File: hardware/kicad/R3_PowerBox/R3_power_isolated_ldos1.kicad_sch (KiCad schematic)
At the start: 12 parts, among them U4 ADM7150ACPZ-3.3-R7, U5 TPS7A2033PDBVR

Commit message: Finalize R3 PowerBox pre-placement corrections
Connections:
- net N$15 is gone; now on net N$14: C44.1, U4.3 (BYP)
- net N$14: no longer C41.1, U4.1 (VREG)
- new net N$13: C41.1, U4.1 (VREG)

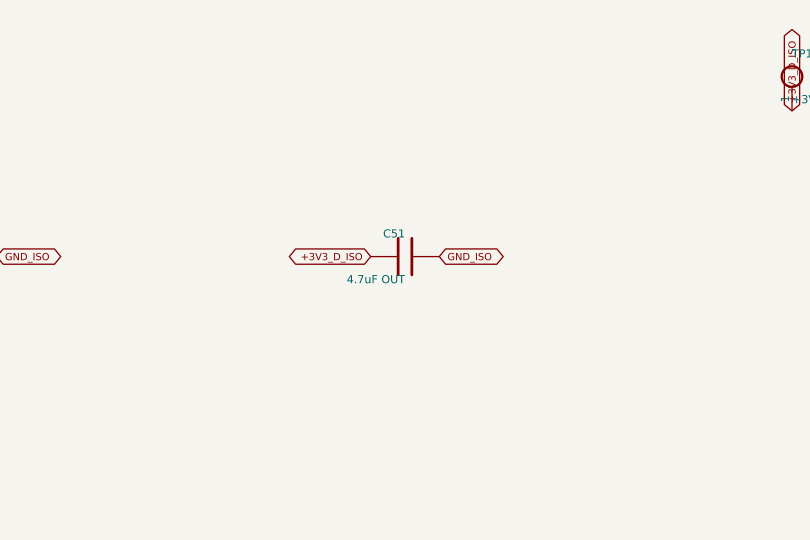
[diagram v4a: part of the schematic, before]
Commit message: Finish R3 PowerBox routing checkpoint F and verification
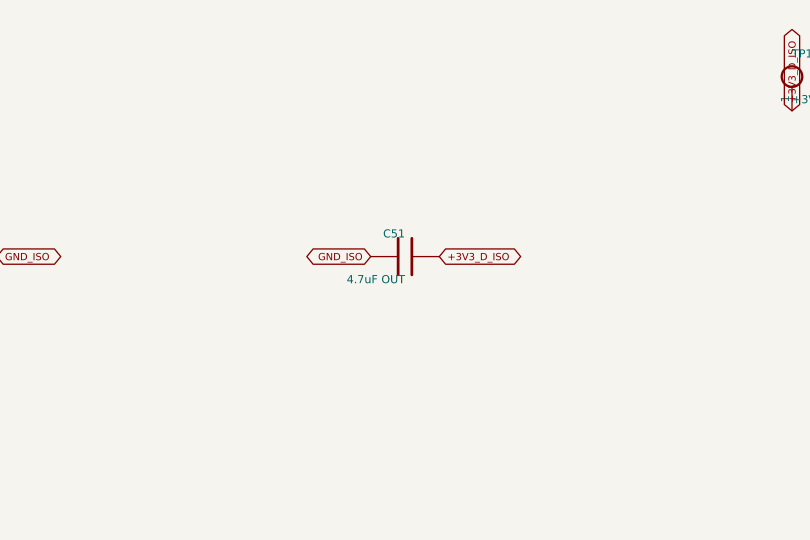
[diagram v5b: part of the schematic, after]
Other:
- moved on the sheet: C51
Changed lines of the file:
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@@
 	(global_label "+3V3_D_ISO"
+		(shape bidirectional)
+		(at 198.81 68 0)
+		(effects
+			(font
+				(size 0.8 0.8)
+			)
+			(justify left)
+		)
+	)
+	(global_label "GND_ISO"
 		(shape bidirectional)
 		(at 191.19 68 180)
@@
 			)
 			(justify right)
-		)
-	)
-	(global_label "GND_ISO"
-		(shape bidirectional)
-		(at 198.81 68 0)
-		(effects
-			(font
-				(size 0.8 0.8)
-			)
-			(justify left)
 		)
 	)
@@
     (instances
       (project "SKiDL-Generated"
-        (path "/9be6bff1-dc85-4a48-94a9-d7223c5e518f/851a1ce1-50e3-53b2-8137-9c4e81a721ef"
+        (path "/c950aac3-a7f8-40a1-8854-63ca2e6194cc/851a1ce1-50e3-53b2-8137-9c4e81a721ef"
           (reference "#FLG0301")
           (unit 1)))))
@@
     (instances
       (project "SKiDL-Generated"
-        (path "/9be6bff1-dc85-4a48-94a9-d7223c5e518f/851a1ce1-50e3-53b2-8137-9c4e81a721ef"
+        (path "/c950aac3-a7f8-40a1-8854-63ca2e6194cc/851a1ce1-50e3-53b2-8137-9c4e81a721ef"
           (reference "#FLG0302")
           (unit 1)))))
@@
     (instances
       (project "SKiDL-Generated"
-        (path "/9be6bff1-dc85-4a48-94a9-d7223c5e518f/851a1ce1-50e3-53b2-8137-9c4e81a721ef"
+        (path "/c950aac3-a7f8-40a1-8854-63ca2e6194cc/851a1ce1-50e3-53b2-8137-9c4e81a721ef"
           (reference "U4")
           (unit 1)))))
@@
     (instances
       (project "SKiDL-Generated"
-        (path "/9be6bff1-dc85-4a48-94a9-d7223c5e518f/851a1ce1-50e3-53b2-8137-9c4e81a721ef"
+        (path "/c950aac3-a7f8-40a1-8854-63ca2e6194cc/851a1ce1-50e3-53b2-8137-9c4e81a721ef"
           (reference "R40")
           (unit 1)))))
@@
     (instances
       (project "SKiDL-Generated"
-        (path "/9be6bff1-dc85-4a48-94a9-d7223c5e518f/851a1ce1-50e3-53b2-8137-9c4e81a721ef"
+        (path "/c950aac3-a7f8-40a1-8854-63ca2e6194cc/851a1ce1-50e3-53b2-8137-9c4e81a721ef"
           (reference "C40")
           (unit 1)))))
@@
     (instances
       (project "SKiDL-Generated"
-        (path "/9be6bff1-dc85-4a48-94a9-d7223c5e518f/851a1ce1-50e3-53b2-8137-9c4e81a721ef"
+        (path "/c950aac3-a7f8-40a1-8854-63ca2e6194cc/851a1ce1-50e3-53b2-8137-9c4e81a721ef"
           (reference "C41")
           (unit 1)))))
@@
     (instances
       (project "SKiDL-Generated"
-        (path "/9be6bff1-dc85-4a48-94a9-d7223c5e518f/851a1ce1-50e3-53b2-8137-9c4e81a721ef"
+        (path "/c950aac3-a7f8-40a1-8854-63ca2e6194cc/851a1ce1-50e3-53b2-8137-9c4e81a721ef"
           (reference "C42")
           (unit 1)))))
@@
     (instances
       (project "SKiDL-Generated"
-        (path "/9be6bff1-dc85-4a48-94a9-d7223c5e518f/851a1ce1-50e3-53b2-8137-9c4e81a721ef"
+        (path "/c950aac3-a7f8-40a1-8854-63ca2e6194cc/851a1ce1-50e3-53b2-8137-9c4e81a721ef"
           (reference "C43")
           (unit 1)))))
@@
     (instances
       (project "SKiDL-Generated"
-        (path "/9be6bff1-dc85-4a48-94a9-d7223c5e518f/851a1ce1-50e3-53b2-8137-9c4e81a721ef"
+        (path "/c950aac3-a7f8-40a1-8854-63ca2e6194cc/851a1ce1-50e3-53b2-8137-9c4e81a721ef"
           (reference "C44")
           (unit 1)))))
@@
     (instances
       (project "SKiDL-Generated"
-        (path "/9be6bff1-dc85-4a48-94a9-d7223c5e518f/851a1ce1-50e3-53b2-8137-9c4e81a721ef"
+        (path "/c950aac3-a7f8-40a1-8854-63ca2e6194cc/851a1ce1-50e3-53b2-8137-9c4e81a721ef"
           (reference "U5")
           (unit 1)))))
@@
     (instances
       (project "SKiDL-Generated"
-        (path "/9be6bff1-dc85-4a48-94a9-d7223c5e518f/851a1ce1-50e3-53b2-8137-9c4e81a721ef"
+        (path "/c950aac3-a7f8-40a1-8854-63ca2e6194cc/851a1ce1-50e3-53b2-8137-9c4e81a721ef"
           (reference "C50")
           (unit 1)))))
   (symbol
     (lib_id "R3_POWER_GEN:C")
-    (at 195 68 90)
+    (at 195 68 270)
     (unit 1)
     (exclude_from_sim no)
@@
     (fields_autoplaced yes)
     (property "Reference" "C51"
-      (at 195 65.46 90)
+      (at 195 65.46 270)
       (effects
         (font
@@
         (justify left)))
     (property "Value" "4.7uF OUT"
-      (at 195 70.54 90)
+      (at 195 70.54 270)
       (effects
         (font
@@
         (justify left)))
     (property "Footprint" "Capacitor_SMD:C_0603_1608Metric"
-      (at 195 68 90)
-      (effects
-        (font
-          (size 0.9 0.9))
-        (hide yes)))
-    (property "Datasheet" "~"
-      (at 195 68 90)
-      (effects
-        (font
-          (size 0.9 0.9))
-        (hide yes)))
-    (property "Description" ""
-      (at 195 68 90)
-      (effects
-        (font
-          (size 0.9 0.9))
-        (hide yes)))
-    (pin "1"
-)
-    (pin "2"
-)
-    (instances
-      (project "SKiDL-Generated"
-        (path "/9be6bff1-dc85-4a48-94a9-d7223c5e518f/851a1ce1-50e3-53b2-8137-9c4e81a721ef"
+      (at 195 68 270)
+      (effects
+        (font
+          (size 0.9 0.9))
+        (hide yes)))
+    (property "Datasheet" "~"
+      (at 195 68 270)
+      (effects
+        (font
+          (size 0.9 0.9))
+        (hide yes)))
+    (property "Description" ""
+      (at 195 68 270)
+      (effects
+        (font
+          (size 0.9 0.9))
+        (hide yes)))
+    (pin "1"
+)
+    (pin "2"
+)
+    (instances
+      (project "SKiDL-Generated"
+        (path "/c950aac3-a7f8-40a1-8854-63ca2e6194cc/851a1ce1-50e3-53b2-8137-9c4e81a721ef"
           (reference "C51")
           (unit 1)))))
@@
     (instances
       (project "SKiDL-Generated"
-        (path "/9be6bff1-dc85-4a48-94a9-d7223c5e518f/851a1ce1-50e3-53b2-8137-9c4e81a721ef"
+        (path "/c950aac3-a7f8-40a1-8854-63ca2e6194cc/851a1ce1-50e3-53b2-8137-9c4e81a721ef"
           (reference "TP11")
           (unit 1)))))
@@
     (instances
       (project "SKiDL-Generated"
-        (path "/9be6bff1-dc85-4a48-94a9-d7223c5e518f/851a1ce1-50e3-53b2-8137-9c4e81a721ef"
+        (path "/c950aac3-a7f8-40a1-8854-63ca2e6194cc/851a1ce1-50e3-53b2-8137-9c4e81a721ef"
           (reference "TP12")
           (unit 1)))))

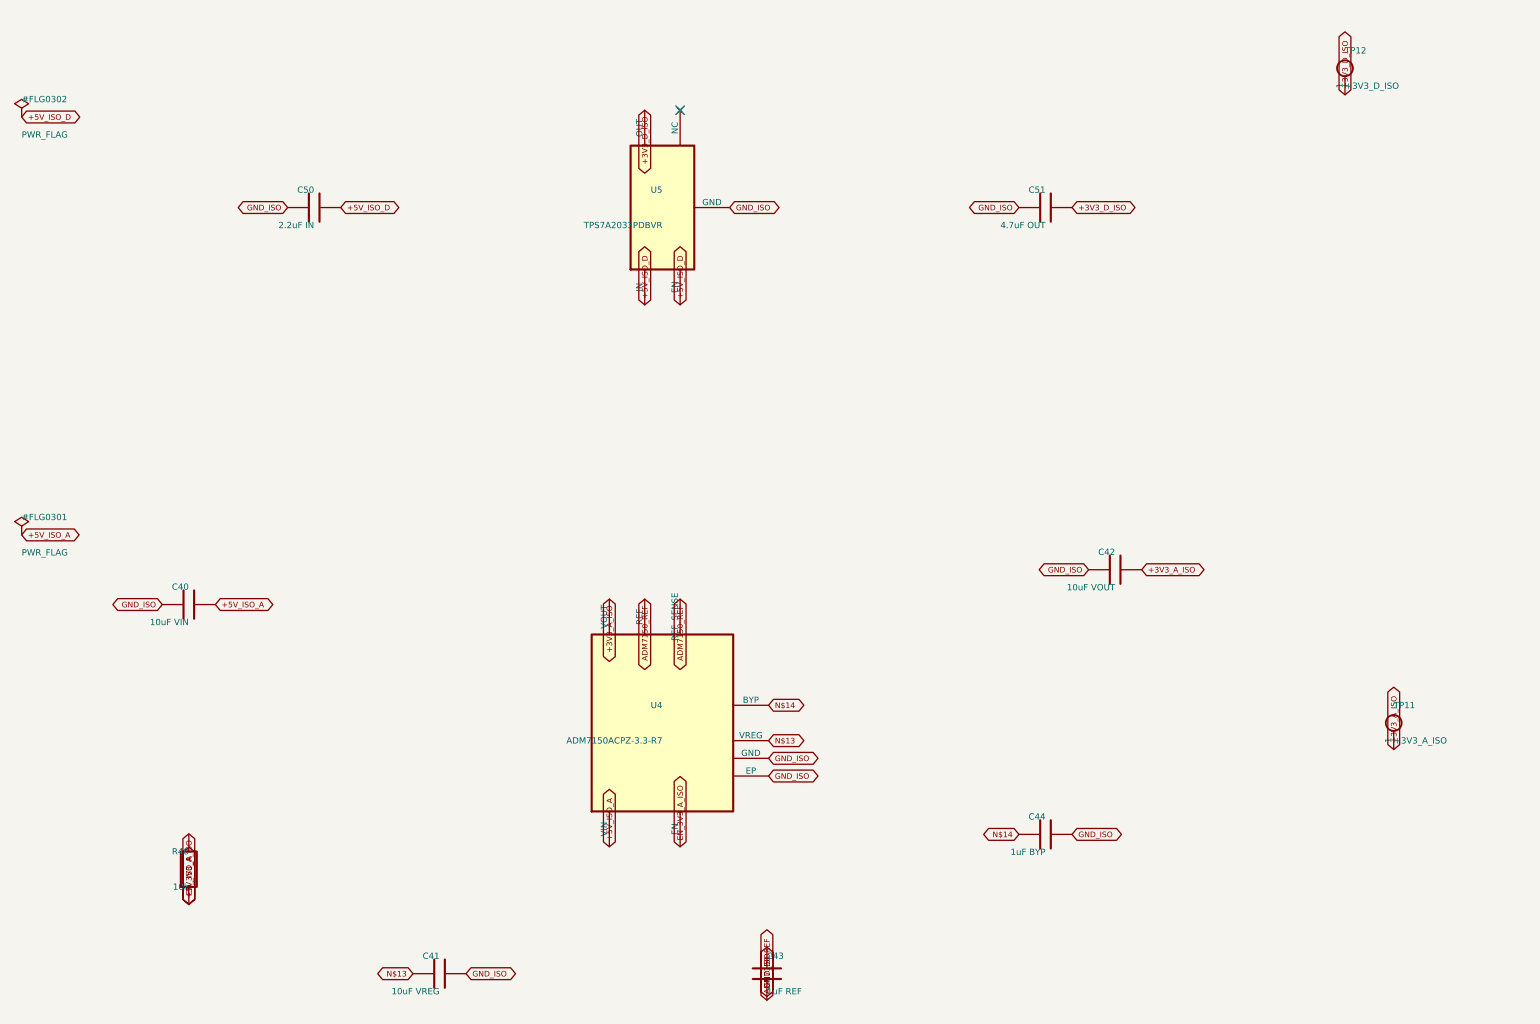
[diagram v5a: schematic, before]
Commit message: Rev.A review fixes: initial schematic and component corrections
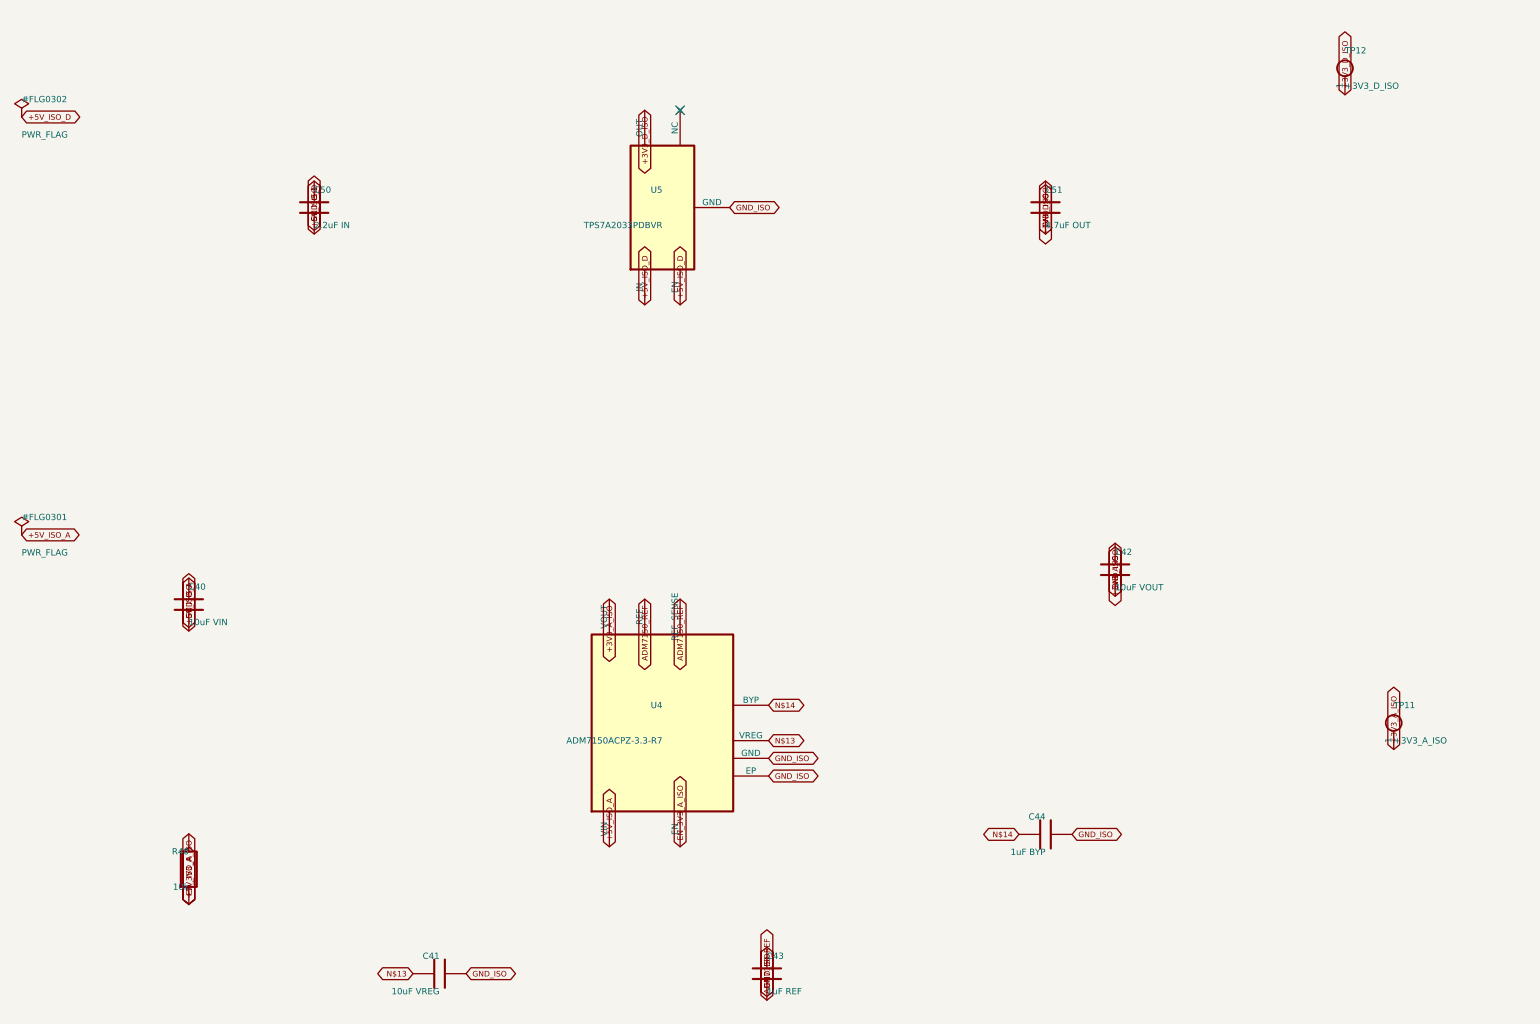
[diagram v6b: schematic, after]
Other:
- moved on the sheet: C40, C42, C50, C51

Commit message: Rev.A review fixes: local charger power-stage reroute checkpoint
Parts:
- C40: value 10uF VIN -> 22uF/25V GRM32ER71E226KE15L; footprint Capacitor_SMD:C_0805_2012Metric -> Capacitor_SMD:C_1210_3225Metric
- C41: value 10uF VREG -> 22uF/25V GRM32ER71E226KE15L; footprint Capacitor_SMD:C_0805_2012Metric -> Capacitor_SMD:C_1210_3225Metric
- C42: value 10uF VOUT -> 22uF/25V GRM32ER71E226KE15L; footprint Capacitor_SMD:C_0805_2012Metric -> Capacitor_SMD:C_1210_3225Metric
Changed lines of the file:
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@@
     (instances
       (project "SKiDL-Generated"
-        (path "/7d40ec76-f97b-4a90-b5ea-ddf1628062b5/851a1ce1-50e3-53b2-8137-9c4e81a721ef"
+        (path "/2b0a7443-ac4c-4207-8273-267cee2a0847/851a1ce1-50e3-53b2-8137-9c4e81a721ef"
           (reference "#FLG0301")
           (unit 1)))))
@@
     (instances
       (project "SKiDL-Generated"
-        (path "/7d40ec76-f97b-4a90-b5ea-ddf1628062b5/851a1ce1-50e3-53b2-8137-9c4e81a721ef"
+        (path "/2b0a7443-ac4c-4207-8273-267cee2a0847/851a1ce1-50e3-53b2-8137-9c4e81a721ef"
           (reference "#FLG0302")
           (unit 1)))))
@@
     (instances
       (project "SKiDL-Generated"
-        (path "/7d40ec76-f97b-4a90-b5ea-ddf1628062b5/851a1ce1-50e3-53b2-8137-9c4e81a721ef"
+        (path "/2b0a7443-ac4c-4207-8273-267cee2a0847/851a1ce1-50e3-53b2-8137-9c4e81a721ef"
           (reference "U4")
           (unit 1)))))
@@
     (instances
       (project "SKiDL-Generated"
-        (path "/7d40ec76-f97b-4a90-b5ea-ddf1628062b5/851a1ce1-50e3-53b2-8137-9c4e81a721ef"
+        (path "/2b0a7443-ac4c-4207-8273-267cee2a0847/851a1ce1-50e3-53b2-8137-9c4e81a721ef"
           (reference "R40")
           (unit 1)))))
@@
           (size 0.9 0.9))
         (justify left)))
-    (property "Value" "10uF VIN"
+    (property "Value" "22uF/25V GRM32ER71E226KE15L"
       (at 72 127.54 0)
       (effects
@@
           (size 0.9 0.9))
         (justify left)))
-    (property "Footprint" "Capacitor_SMD:C_0805_2012Metric"
+    (property "Footprint" "Capacitor_SMD:C_1210_3225Metric"
       (at 72 125 0)
       (effects
@@
     (instances
       (project "SKiDL-Generated"
-        (path "/7d40ec76-f97b-4a90-b5ea-ddf1628062b5/851a1ce1-50e3-53b2-8137-9c4e81a721ef"
+        (path "/2b0a7443-ac4c-4207-8273-267cee2a0847/851a1ce1-50e3-53b2-8137-9c4e81a721ef"
           (reference "C40")
           (unit 1)))))
@@
           (size 0.9 0.9))
         (justify left)))
-    (property "Value" "10uF VREG"
+    (property "Value" "22uF/25V GRM32ER71E226KE15L"
       (at 108 180.54 90)
       (effects
@@
           (size 0.9 0.9))
         (justify left)))
-    (property "Footprint" "Capacitor_SMD:C_0805_2012Metric"
+    (property "Footprint" "Capacitor_SMD:C_1210_3225Metric"
       (at 108 178 90)
       (effects
@@
     (instances
       (project "SKiDL-Generated"
-        (path "/7d40ec76-f97b-4a90-b5ea-ddf1628062b5/851a1ce1-50e3-53b2-8137-9c4e81a721ef"
+        (path "/2b0a7443-ac4c-4207-8273-267cee2a0847/851a1ce1-50e3-53b2-8137-9c4e81a721ef"
           (reference "C41")
           (unit 1)))))
@@
           (size 0.9 0.9))
         (justify left)))
-    (property "Value" "10uF VOUT"
+    (property "Value" "22uF/25V GRM32ER71E226KE15L"
       (at 205 122.54 0)
       (effects
@@
           (size 0.9 0.9))
         (justify left)))
-    (property "Footprint" "Capacitor_SMD:C_0805_2012Metric"
+    (property "Footprint" "Capacitor_SMD:C_1210_3225Metric"
       (at 205 120 0)
       (effects
@@
     (instances
       (project "SKiDL-Generated"
-        (path "/7d40ec76-f97b-4a90-b5ea-ddf1628062b5/851a1ce1-50e3-53b2-8137-9c4e81a721ef"
+        (path "/2b0a7443-ac4c-4207-8273-267cee2a0847/851a1ce1-50e3-53b2-8137-9c4e81a721ef"
           (reference "C42")
           (unit 1)))))
@@
     (instances
       (project "SKiDL-Generated"
-        (path "/7d40ec76-f97b-4a90-b5ea-ddf1628062b5/851a1ce1-50e3-53b2-8137-9c4e81a721ef"
+        (path "/2b0a7443-ac4c-4207-8273-267cee2a0847/851a1ce1-50e3-53b2-8137-9c4e81a721ef"
           (reference "C43")
           (unit 1)))))
@@
     (instances
       (project "SKiDL-Generated"
-        (path "/7d40ec76-f97b-4a90-b5ea-ddf1628062b5/851a1ce1-50e3-53b2-8137-9c4e81a721ef"
+        (path "/2b0a7443-ac4c-4207-8273-267cee2a0847/851a1ce1-50e3-53b2-8137-9c4e81a721ef"
           (reference "C44")
           (unit 1)))))
@@
     (instances
       (project "SKiDL-Generated"
-        (path "/7d40ec76-f97b-4a90-b5ea-ddf1628062b5/851a1ce1-50e3-53b2-8137-9c4e81a721ef"
+        (path "/2b0a7443-ac4c-4207-8273-267cee2a0847/851a1ce1-50e3-53b2-8137-9c4e81a721ef"
           (reference "U5")
           (unit 1)))))
@@
     (instances
       (project "SKiDL-Generated"
-        (path "/7d40ec76-f97b-4a90-b5ea-ddf1628062b5/851a1ce1-50e3-53b2-8137-9c4e81a721ef"
+        (path "/2b0a7443-ac4c-4207-8273-267cee2a0847/851a1ce1-50e3-53b2-8137-9c4e81a721ef"
           (reference "C50")
           (unit 1)))))
@@
     (instances
       (project "SKiDL-Generated"
-        (path "/7d40ec76-f97b-4a90-b5ea-ddf1628062b5/851a1ce1-50e3-53b2-8137-9c4e81a721ef"
+        (path "/2b0a7443-ac4c-4207-8273-267cee2a0847/851a1ce1-50e3-53b2-8137-9c4e81a721ef"
           (reference "C51")
           (unit 1)))))
@@
     (instances
       (project "SKiDL-Generated"
-        (path "/7d40ec76-f97b-4a90-b5ea-ddf1628062b5/851a1ce1-50e3-53b2-8137-9c4e81a721ef"
+        (path "/2b0a7443-ac4c-4207-8273-267cee2a0847/851a1ce1-50e3-53b2-8137-9c4e81a721ef"
           (reference "TP11")
           (unit 1)))))
@@
     (instances
       (project "SKiDL-Generated"
-        (path "/7d40ec76-f97b-4a90-b5ea-ddf1628062b5/851a1ce1-50e3-53b2-8137-9c4e81a721ef"
+        (path "/2b0a7443-ac4c-4207-8273-267cee2a0847/851a1ce1-50e3-53b2-8137-9c4e81a721ef"
           (reference "TP12")
           (unit 1)))))
